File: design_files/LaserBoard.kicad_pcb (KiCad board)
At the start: 2 copper layers, 76 x 95 mm, 111 parts, among them J1 Conn_01x03_Socket, J10 DA15_Receptacle, J11 DB25_Receptacle, J12 RJ45_Amphenol_RJMG1BD3B8K1ANR, J13 Conn_01x06, J14 Conn_01x02_Pin, J15 Conn_01x03, J17 Screw_Terminal_01x02, J18 Screw_Terminal_01x02, J2 Conn_01x03_Socket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

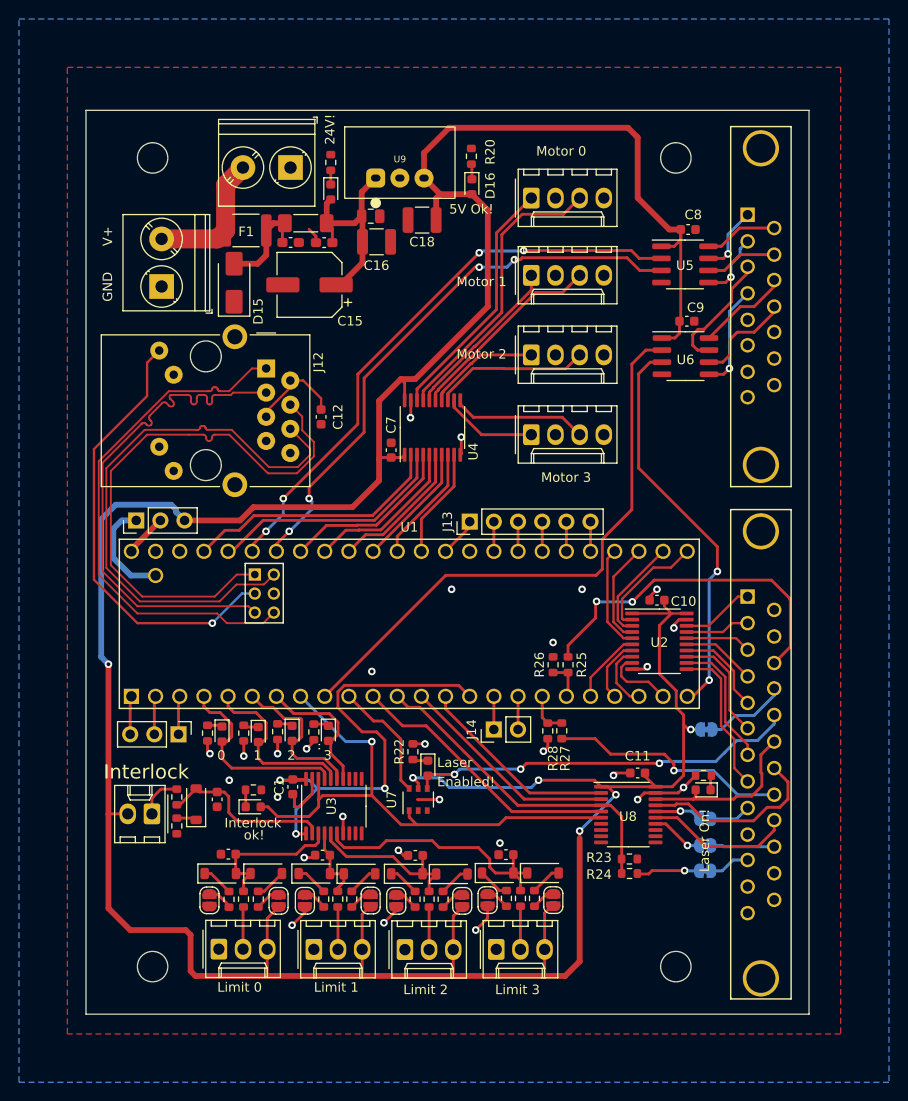
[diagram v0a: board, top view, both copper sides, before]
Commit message: And that's why we write documentation - two small errors on the pcb
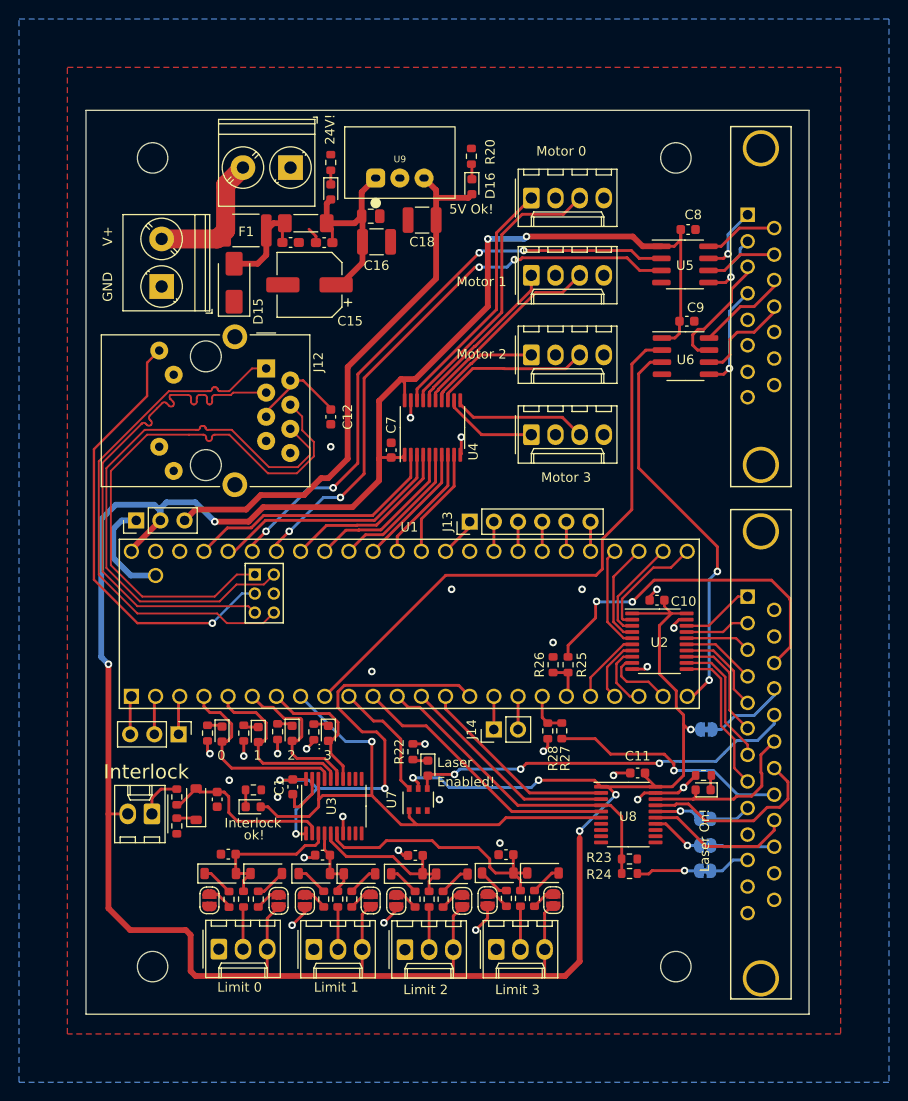
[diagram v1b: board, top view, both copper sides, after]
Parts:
- moved C12 1.02 mm to (93.7, 67.2)
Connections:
- C18 pad 1: +5V -> 5V_SUPPLY
- D16 pad 2: +5V -> 5V_SUPPLY
- JP12 pad 2: Net-(JP12-C) -> +5V
- JP12 pad 3: +5V -> 5V_SUPPLY
- U1 pad 48: Net-(JP12-C) -> +5V
- U7 pad 3: unconnected-(U7-Pad3) -> GND
- U9 pad 3: +5V -> 5V_SUPPLY
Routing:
- net 5V_SUPPLY: track 0.00 -> 57.8 mm
- net +5V: track 349.9 -> 323.1 mm, vias 6 -> 9
- net Net-(JP12-C): track 4.51 -> 0.00 mm
- net GND: track 47.9 -> 45.6 mm, vias 28 -> 29
- net GALVO_CLOCK: track 60.9 -> 62.3 mm
- net GALVO_SYNC: track 59.3 -> 60.1 mm

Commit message: BOM, readme update
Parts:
- C1, C10, C11, C7, C8, C9: value 0.1uF, 16V -> 0.1uF, 25V
- C12: value 0.1uF, 16V -> 0.1uF, 50V
- C13, C14: footprint LaserBoardR5:C_0603_1608Metric_Pad1.08x0.95mm_HandSolder -> LaserBoardR5:C_0603_1608Metric
- J1, J2, J3, J4: value Conn_01x03_Socket -> Type KK 1x03 Socket
- J5: value Conn_01x02_Socket -> Type KK 1x02 Socket
- J6, J7, J8, J9: value Conn_01x04_Socket -> Type KK 1x04 Socket
- JP1, JP10, JP2, JP3, JP4, JP5, JP6, JP7, JP8: value Jumper_2_Open -> Jumper 2 Position, Open
- JP11, JP13, JP9: value e -> Jumper 2 Position, Closed
- JP12: value SolderJumper_3_Open -> Jumper 3 Position, Open
- moved J18 5.00 mm to (75.9, 48.5), turned to -90 degrees
- moved J5 2.54 mm to (72.4, 109.0), turned to 0 degrees
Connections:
- J18 pad 1: GND -> V_INPUT
- J18 pad 2: V_INPUT -> GND
- J5 pad 1: Net-(J5-Pin_1) -> +5V
- J5 pad 2: +5V -> Net-(J5-Pin_2)
- R15 pad 1: Net-(J5-Pin_1) -> Net-(J5-Pin_2)
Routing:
- net Net-(J5-Pin_2): track 0.00 -> 4.66 mm
- net Net-(J5-Pin_1): track 4.66 -> 0.00 mm

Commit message: Rev 5a
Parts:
- added JP14: Jumper_2_Bridged, LaserBoardR5:SolderJumper-2_P1.3mm_Bridged_RoundedPad1.0x1.5mm, B.Cu at (87.0, 118.0)
- added JP15: Jumper_2_Bridged, LaserBoardR5:SolderJumper-2_P1.3mm_Bridged_RoundedPad1.0x1.5mm, B.Cu at (87.0, 115.0)
- added JP16: Jumper 2 Position, Open, LaserBoardR5:SolderJumper-2_P1.3mm_Open_RoundedPad1.0x1.5mm, B.Cu at (92.0, 115.0)
- added JP17: Jumper_2_Bridged, LaserBoardR5:SolderJumper-2_P1.3mm_Bridged_RoundedPad1.0x1.5mm, B.Cu at (97.0, 115.0)
- added JP18: Jumper 2 Position, Open, LaserBoardR5:SolderJumper-2_P1.3mm_Open_RoundedPad1.0x1.5mm, B.Cu at (102.0, 115.0)
- added JP19: Jumper_2_Bridged, LaserBoardR5:SolderJumper-2_P1.3mm_Bridged_RoundedPad1.0x1.5mm, B.Cu at (107.0, 115.0)
- added JP20: Jumper 2 Position, Open, LaserBoardR5:SolderJumper-2_P1.3mm_Open_RoundedPad1.0x1.5mm, B.Cu at (112.0, 115.0)
- added JP21: Jumper_2_Bridged, LaserBoardR5:SolderJumper-2_P1.3mm_Bridged_RoundedPad1.0x1.5mm, B.Cu at (117.0, 115.0)
- added R30: R10K, LaserBoardR5:R_0603_1608Metric, F.Cu at (99.0, 93.1)
- added R31: R10K, LaserBoardR5:R_0603_1608Metric, F.Cu at (100.6, 93.1)
- added R32: R10K, LaserBoardR5:R_0603_1608Metric, F.Cu at (102.2, 93.1)
- added R33: R10K, LaserBoardR5:R_0603_1608Metric, F.Cu at (103.8, 93.1)
- C15: footprint LaserBoardR5:CP_Elec_6.3x9.9 -> Capacitor_THT:CP_Radial_D6.3mm_P2.50mm
- JP1, JP2, JP4, JP6, JP8: moved to B.Cu
- JP3, JP5, JP7: value Jumper 2 Position, Open -> Jumper_2_Bridged; footprint LaserBoardR5:SolderJumper-2_P1.3mm_Open_RoundedPad1.0x1.5mm -> LaserBoardR5:SolderJumper-2_P1.3mm_Bridged_RoundedPad1.0x1.5mm; moved to B.Cu
- U5, U6: value UA9638CD -> UA9638CDR
- moved JP1 6.96 mm to (82.0, 115.0), turned to 0 degrees
- moved C15 4.56 mm to (96.0, 54.0)
- moved J10 2.36 mm to (136.8, 54.9)
- moved R9 2.31 mm to (117.4, 117.3), turned to 180 degrees
- moved C8 2.19 mm to (129.4, 46.4)
- moved U5 2.19 mm to (129.1, 50.0)
- moved C9 2.19 mm to (129.3, 56.0)
- moved U6 2.19 mm to (129.2, 59.7)
- moved R7 2.04 mm to (107.4, 117.1), turned to 180 degrees
- moved JP8 1.79 mm to (112.0, 118.0), turned to 0 degrees
- moved R4 1.57 mm to (97.4, 117.3), turned to 180 degrees
- moved R2 1.41 mm to (87.4, 117.3), turned to 180 degrees
- moved JP6 1.39 mm to (102.0, 118.0), turned to 0 degrees
- moved R3 1.36 mm to (81.8, 117.3), turned to 0 degrees
- moved R5 1.31 mm to (91.8, 117.3), turned to 0 degrees
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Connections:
- C12 pad 1: Net-(J12-RCT) -> GND
- C12 pad 2: GND -> Net-(J12-RCT)
- J12 pad L1: unconnected-(J12-LEDY_A-PadL1) -> GND
- J12 pad L2: unconnected-(J12-LEDY_K-PadL2) -> Net-(J12-LEDY_K)
- J12 pad L3: GND -> unconnected-(J12-LEDG_K-PadL3)
- J12 pad L4: Net-(J12-LEDG_A) -> unconnected-(J12-LEDG_A-PadL4)
- J5 pad 2: Net-(J5-Pin_2) -> Net-(D10-K)
- JP1 pad 1: Net-(JP1-A) -> Net-(D2-K)
- JP1 pad 2: +5V -> Net-(J1-Pin_2)
- JP3 pad 1: Net-(JP3-A) -> +5V
- JP3 pad 2: +5V -> Net-(JP3-B)
- JP5 pad 1: Net-(JP5-A) -> +5V
- JP5 pad 2: +5V -> Net-(JP5-B)
- JP7 pad 1: Net-(JP7-A) -> +5V
- JP7 pad 2: +5V -> Net-(JP7-B)
- R15 pad 1: Net-(J5-Pin_2) -> Net-(D10-K)
- R2 pad 1: Net-(JP1-A) -> Net-(JP14-B)
- R4 pad 1: Net-(JP3-A) -> Net-(JP3-B)
- R7 pad 1: Net-(JP5-A) -> Net-(JP5-B)
- R9 pad 1: Net-(JP7-A) -> Net-(JP7-B)
- U1 pad 61: Net-(J12-LEDG_A) -> Net-(J12-LEDY_K)
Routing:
- net GND: track 45.6 -> 94.6 mm, vias 29 -> 36
- net Net-(J12-LEDG_A): track 47.0 -> 0.00 mm, vias 1 -> 0
- net Net-(J12-LEDY_K): track 0.00 -> 32.0 mm, vias 0 -> 1
- net Net-(J1-Pin_2): track 4.46 -> 15.7 mm
- net Net-(J2-Pin_2): track 4.47 -> 15.6 mm
- net Net-(J3-Pin_2): track 4.48 -> 15.6 mm
- net Net-(J4-Pin_2): track 4.53 -> 15.6 mm
- net Net-(D10-K): track 2.11 -> 9.56 mm
- net +3.3V: track 48.7 -> 55.6 mm
- net Net-(JP7-B): track 0.00 -> 4.93 mm, vias 0 -> 1
- net Net-(JP14-B): track 0.00 -> 4.93 mm, vias 0 -> 1
- net Net-(JP5-B): track 0.00 -> 4.89 mm, vias 0 -> 1
- net ENABLE: track 12.9 -> 17.6 mm
- net Net-(JP3-B): track 0.00 -> 4.69 mm, vias 0 -> 1
- net Net-(D7-A): track 3.30 -> 7.99 mm, vias 0 -> 1
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- removed copper zone on F.Cu, net GND
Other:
- board size 76 x 95 mm -> 80 x 95 mm
- board text added: "5V!"
- board text added: "r5a - msds - 2023"
- board text removed: "5V Ok!"
- board text removed: "r5 - msds - 2023"

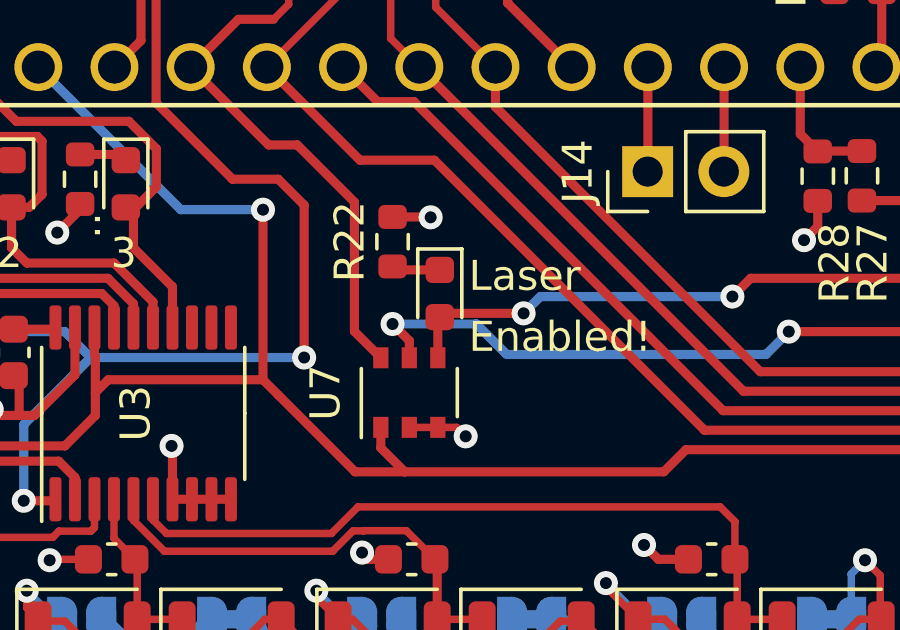
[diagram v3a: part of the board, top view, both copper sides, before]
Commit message: Add new images, purge an old schematic sheet, and update the package of a component to match the datasheet.
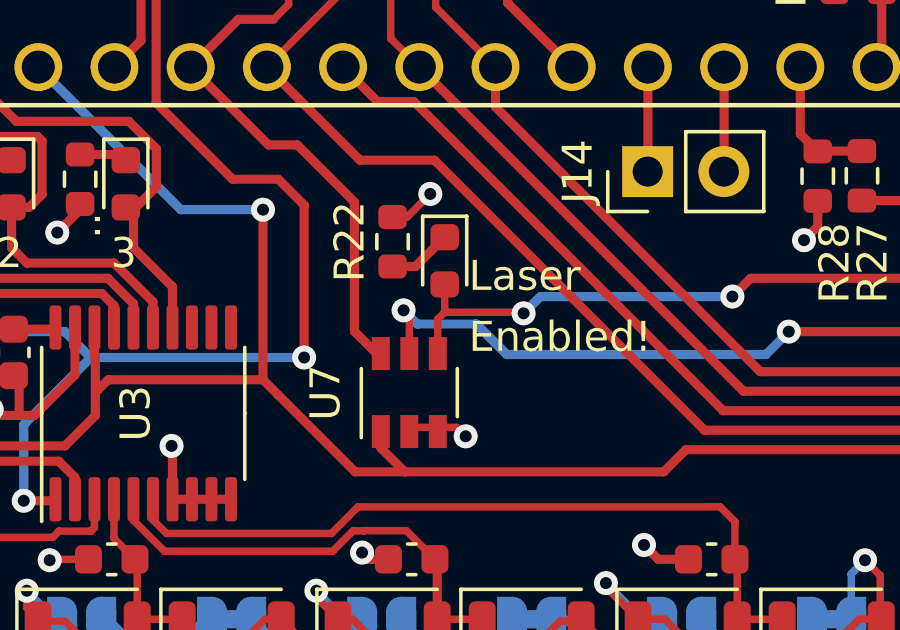
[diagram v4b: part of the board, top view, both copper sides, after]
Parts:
- moved D18 1.10 mm to (104.1, 103.0)
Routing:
- net SAFE_ENABLE: track 41.0 -> 41.8 mm
- net Net-(D18-K): track 1.62 -> 2.14 mm
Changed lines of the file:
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@@
     (fp_line (start 0.825 1.525) (end -0.825 1.525)
       (stroke (width 0.1) (type solid)) (layer "F.Fab"))
-    (pad "1" smd rect (at -1.16 -0.95 90) (size 0.7 0.51) (layers "F.Cu" "F.Paste" "F.Mask")
+    (pad "1" smd rect (at -1.3 -0.95 90) (size 1.1 0.6) (layers "F.Cu" "F.Paste" "F.Mask")
       (net 20 "INTERLOCK") (pintype "input"))
-    (pad "2" smd rect (at -1.16 0 90) (size 0.7 0.51) (layers "F.Cu" "F.Paste" "F.Mask")
+    (pad "2" smd rect (at -1.3 0 90) (size 1.1 0.6) (layers "F.Cu" "F.Paste" "F.Mask")
       (net 1 "GND") (pinfunction "GND") (pintype "power_in"))
-    (pad "3" smd rect (at -1.16 0.95 90) (size 0.7 0.51) (layers "F.Cu" "F.Paste" "F.Mask")
+    (pad "3" smd rect (at -1.3 0.95 90) (size 1.1 0.6) (layers "F.Cu" "F.Paste" "F.Mask")
       (net 1 "GND") (pintype "input"))
-    (pad "4" smd rect (at 1.16 0.95 90) (size 0.7 0.51) (layers "F.Cu" "F.Paste" "F.Mask")
+    (pad "4" smd rect (at 1.3 0.95 90) (size 1.1 0.6) (layers "F.Cu" "F.Paste" "F.Mask")
       (net 29 "SAFE_ENABLE") (pintype "output"))
-    (pad "5" smd rect (at 1.16 0 90) (size 0.7 0.51) (layers "F.Cu" "F.Paste" "F.Mask")
+    (pad "5" smd rect (at 1.3 0 90) (size 1.1 0.6) (layers "F.Cu" "F.Paste" "F.Mask")
       (net 8 "+5V") (pinfunction "VCC") (pintype "power_in"))
-    (pad "6" smd rect (at 1.16 -0.95 90) (size 0.7 0.51) (layers "F.Cu" "F.Paste" "F.Mask")
+    (pad "6" smd rect (at 1.3 -0.95 90) (size 1.1 0.6) (layers "F.Cu" "F.Paste" "F.Mask")
       (net 114 "ENABLE") (pintype "input"))
     (model "${KICAD6_3DMODEL_DIR}/Package_SO.3dshapes/TSOP-6_1.65x3.05mm_P0.95mm.wrl"
@@
   )
   (footprint "LaserBoardR5:LED_0603_1608Metric" (layer "F.Cu")
-    (at 103.9368 104.14 -90)
+    (at 104.1 103.05 -90)
     (descr "LED SMD 0603 (1608 Metric), square (rectangular) end terminal, IPC_7351 nominal, (Body size source: http://www.tortai-tech.com/upload/download/2011102023233369053.pdf), generated with kicad-footprint-generator")
     (tags "LED")
@@
   (segment (start 132.08 104.902) (end 130.81 106.172) (width 0.3048) (layer "F.Cu") (net 1))
   (segment (start 122.1375 112.8625) (end 122.1 112.9) (width 0.25) (layer "F.Cu") (net 1))
+  (segment (start 102.362 101.5878) (end 102.8522 101.5878) (width 0.25) (layer "F.Cu") (net 1))
   (segment (start 84.582 101.281) (end 84.582 102.87) (width 0.3048) (layer "F.Cu") (net 1))
+  (segment (start 102.8522 101.5878) (end 103.62 100.82) (width 0.25) (layer "F.Cu") (net 1))
   (segment (start 126.68 106.746) (end 125.984 107.442) (width 0.3048) (layer "F.Cu") (net 1))
   (segment (start 93.726 67.9964) (end 93.726 69.3) (width 0.25) (layer "F.Cu") (net 1))
-  (segment (start 103.6198 101.5878) (end 103.632 101.6) (width 0.3048) (layer "F.Cu") (net 1))
   (segment (start 122.1375 109.996) (end 122.1375 110.646) (width 0.25) (layer "F.Cu") (net 1))
   (segment (start 131 56) (end 131.1 56.1) (width 0.25) (layer "F.Cu") (net 1))
@@
   (segment (start 81.8 109.4) (end 81.8 108.209) (width 0.25) (layer "F.Cu") (net 1))
   (segment (start 93.726 39.6504) (end 93.726 38.326) (width 0.25) (layer "F.Cu") (net 1))
-  (segment (start 102.362 101.5878) (end 103.6198 101.5878) (width 0.3048) (layer "F.Cu") (net 1))
   (segment (start 91.776 105.273) (end 91.776 106.852) (width 0.3048) (layer "F.Cu") (net 1))
   (segment (start 91.948 101.346) (end 91.186 102.108) (width 0.3048) (layer "F.Cu") (net 1))
@@
   (via (at 131.1 56.1) (size 0.8) (drill 0.4) (layers "F.Cu" "B.Cu") (net 1))
   (via (at 123.444 104.902) (size 0.8) (drill 0.4) (layers "F.Cu" "B.Cu") (net 1))
-  (via (at 103.632 101.6) (size 0.8) (drill 0.4) (layers "F.Cu" "B.Cu") (net 1))
+  (via (at 103.62 100.82) (size 0.8) (drill 0.4) (layers "F.Cu" "B.Cu") (net 1))
   (via (at 108.5 37.6) (size 0.8) (drill 0.4) (layers "F.Cu" "B.Cu") (net 1))
   (via (at 105.1 92.3) (size 0.8) (drill 0.4) (layers "F.Cu" "B.Cu") (net 1))
@@
   (segment (start 115.57 105.41) (end 121.4515 105.41) (width 0.3048) (layer "F.Cu") (net 8))
   (segment (start 131.572 100.076) (end 131.318 100.076) (width 0.3048) (layer "F.Cu") (net 8))
-  (segment (start 102.9208 105.7148) (end 102.362 105.156) (width 0.3048) (layer "F.Cu") (net 8))
   (segment (start 72.644 121.158) (end 78.486 121.158) (width 0.6096) (layer "F.Cu") (net 8))
-  (segment (start 102.9208 106.282) (end 102.9208 105.7148) (width 0.3048) (layer "F.Cu") (net 8))
   (segment (start 86.614 76.708) (end 85.09 78.232) (width 0.6096) (layer "F.Cu") (net 8))
   (segment (start 117.08 125.97) (end 117.08 123) (width 0.6096) (layer "F.Cu") (net 8))
   (segment (start 97.08 123) (end 97.08 125.932) (width 0.6096) (layer "F.Cu") (net 8))
   (segment (start 102.616 63.246) (end 110.236 55.626) (width 0.6096) (layer "F.Cu") (net 8))
+  (segment (start 102.9208 104.8908) (end 102.73 104.7) (width 0.25) (layer "F.Cu") (net 8))
   (segment (start 131.318 100.076) (end 130.81 99.568) (width 0.3048) (layer "F.Cu") (net 8))
   (segment (start 101.4906 65.4765) (end 101.4906 63.6446) (width 0.3048) (layer "F.Cu") (net 8))
@@
   (segment (start 129.54 87.88) (end 131.1325 87.88) (width 0.25) (layer "F.Cu") (net 8))
   (segment (start 119.888 110.744) (end 119.888 111.506) (width 0.3048) (layer "F.Cu") (net 8))
+  (segment (start 102.9208 106.142) (end 102.9208 104.8908) (width 0.25) (layer "F.Cu") (net 8))
   (segment (start 121.4515 105.41) (end 122.1375 106.096) (width 0.3048) (layer "F.Cu") (net 8))
   (segment (start 122.1375 106.096) (end 122.86479 106.096) (width 0.3048) (layer "F.Cu") (net 8))
@@
   (segment (start 126.759 104.648) (end 126.759 104.9925) (width 0.3048) (layer "F.Cu") (net 8))
   (via (at 131.572 100.076) (size 0.8) (drill 0.4) (layers "F.Cu" "B.Cu") (net 8))
-  (via (at 102.362 105.156) (size 0.8) (drill 0.4) (layers "F.Cu" "B.Cu") (net 8))
+  (via (at 102.73 104.7) (size 0.8) (drill 0.4) (layers "F.Cu" "B.Cu") (net 8))
   (via (at 114.3 48.26) (size 0.8) (drill 0.4) (layers "F.Cu" "B.Cu") (net 8))
   (via (at 70.358 93.218) (size 0.8) (drill 0.4) (layers "F.Cu" "B.Cu") (net 8))
@@
   (segment (start 114.808 106.172) (end 115.57 105.41) (width 0.3048) (layer "B.Cu") (net 8))
   (segment (start 87.08 120.184) (end 87.63 119.634) (width 0.25) (layer "B.Cu") (net 8))
+  (segment (start 105.156 105.156) (end 103.186 105.156) (width 0.3048) (layer "B.Cu") (net 8))
   (segment (start 75.184 76.454) (end 75.819 77.089) (width 0.6096) (layer "B.Cu") (net 8))
   (segment (start 107.08 121.52) (end 107.08 123) (width 0.3048) (layer "B.Cu") (net 8))
+  (segment (start 103.186 105.156) (end 102.73 104.7) (width 0.3048) (layer "B.Cu") (net 8))
   (segment (start 97.08 121.106) (end 97.08 123) (width 0.25) (layer "B.Cu") (net 8))
   (segment (start 76.454 76.2) (end 79.502 76.2) (width 0.6096) (layer "B.Cu") (net 8))
@@
   (segment (start 106.172 106.172) (end 114.808 106.172) (width 0.3048) (layer "B.Cu") (net 8))
   (segment (start 114.046 48.514) (end 114.3 48.26) (width 0.6096) (layer "B.Cu") (net 8))
-  (segment (start 102.362 105.156) (end 105.156 105.156) (width 0.3048) (layer "B.Cu") (net 8))
   (segment (start 75.819 78.105) (end 75.819 77.089) (width 0.6096) (layer "B.Cu") (net 8))
   (segment (start 75.819 78.105) (end 75.819 76.835) (width 0.6096) (layer "B.Cu") (net 8))
@@
   (segment (start 108.5596 40.703) (end 108.5088 40.6522) (width 0.3048) (layer "F.Cu") (net 26))
   (segment (start 93.726 41.3004) (end 93.726 42.7867) (width 0.3048) (layer "F.Cu") (net 27))
-  (segment (start 103.9368 103.3525) (end 102.4767 103.3525) (width 0.3048) (layer "F.Cu") (net 28))
-  (segment (start 102.4767 103.3525) (end 102.362 103.2378) (width 0.3048) (layer "F.Cu") (net 28))
-  (segment (start 103.8708 104.9935) (end 103.9368 104.9275) (width 0.3048) (layer "F.Cu") (net 29))
+  (segment (start 102.362 103.2378) (end 103.1247 103.2378) (width 0.3048) (layer "F.Cu") (net 28))
+  (segment (start 103.1247 103.2378) (end 104.1 102.2625) (width 0.3048) (layer "F.Cu") (net 28))
+  (segment (start 103.8708 106.142) (end 103.8708 104.9935) (width 0.25) (layer "F.Cu") (net 29))
   (segment (start 128.27 103.632) (end 114.3 103.632) (width 0.3048) (layer "F.Cu") (net 29))
-  (segment (start 103.8708 106.282) (end 103.8708 104.9935) (width 0.3048) (layer "F.Cu") (net 29))
-  (segment (start 106.7308 104.8004) (end 104.0639 104.8004) (width 0.3048) (layer "F.Cu") (net 29))
+  (segment (start 103.8708 104.9935) (end 104.1 104.7643) (width 0.25) (layer "F.Cu") (net 29))
+  (segment (start 104.1 103.8375) (end 104.1 104.7643) (width 0.25) (layer "F.Cu") (net 29))
+  (segment (start 104.1 104.7643) (end 106.6947 104.7643) (width 0.25) (layer "F.Cu") (net 29))
   (segment (start 114.3 103.632) (end 113.6904 104.2416) (width 0.3048) (layer "F.Cu") (net 29))
-  (segment (start 104.0639 104.8004) (end 103.9368 104.9275) (width 0.3048) (layer "F.Cu") (net 29))
+  (segment (start 106.6947 104.7643) (end 106.7308 104.8004) (width 0.25) (layer "F.Cu") (net 29))
   (via (at 106.7308 104.8004) (size 0.8) (drill 0.4) (layers "F.Cu" "B.Cu") (net 29))
   (via (at 128.27 103.632) (size 0.8) (drill 0.4) (layers "F.Cu" "B.Cu") (net 29))
